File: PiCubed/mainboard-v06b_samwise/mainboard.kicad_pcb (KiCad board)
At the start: 4 copper layers, 90.2 x 95.9 mm, 204 parts, among them J1 503182-1852, J10 35362-0450, J11 MPPT board, J12 35362-0550, J13 USB_C_pycubed, J14 Conn_01x06_Horizontal, J15 35362-0550, J16 1985807, J17 35362-0450, J18 1985807, J19 35362-0650, J2 Conn_ARM_JTAG_SWD_10, J20 35362-0750, J21 35362-0750, J22 QWIIC, J3 35362-0850, J4 35362-0850, J5 35362-1050, J6 35362-0950, J7 Amphenol_901-144, J8 1985807, J9 1985807, Q1 BSS138DWQ-7, Q10 DMP2040USS-13, Q11 MMDT2907, Q15 MBT2222ADW1T1, Q16 MBT2222ADW1T1, Q18 BSS138DWQ-7, Q19 BSS138DWQ-7, Q2 MBT2222ADW1T1, Q21 DMP2040USS-13, Q3 MBT2222ADW1T1, Q4 MBT2222ADW1T1, Q5 IRLML2803, Q6 MMBT2222A-TP, Q7 BSS138DWQ-7, Q8 MBT2222ADW1T1, Q9 IRLML2803, SW1 KMR231NG LFS, U1 MAX706RESA, U16 PE014006, U17 BQ25883RGER, U2 ATSAMD51J20A-AF, U21 TPS7A4501DCQT, U23 RFM98PW, U4 ADM1176-1ARMZ-R7, U5 TPS54226PWPR, U6 LT3652HVIMSE#PBF, U8 MR25H40MDF, Y1 32.768kHz

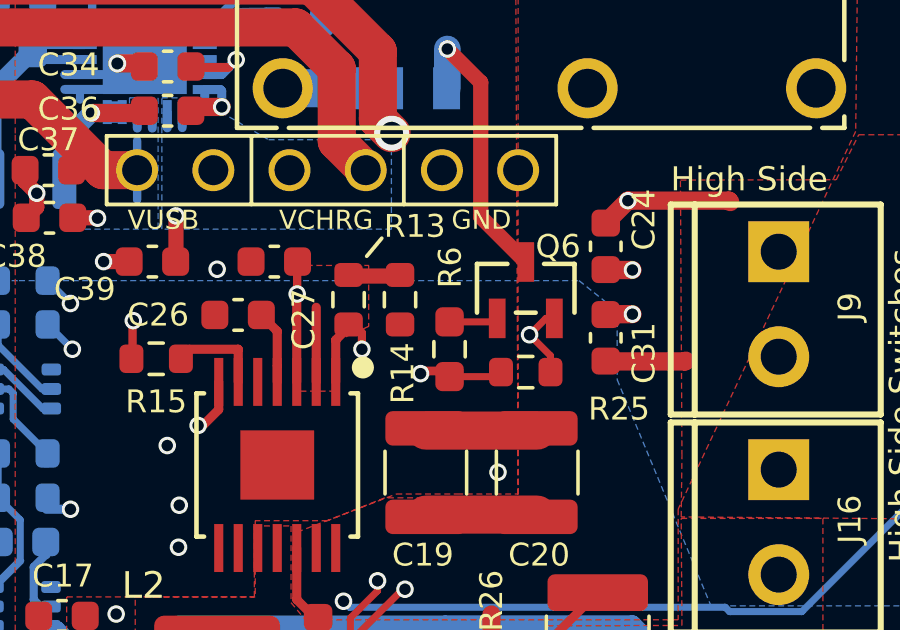
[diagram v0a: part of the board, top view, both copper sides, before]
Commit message: updated interface board, Picubed resistor footprints
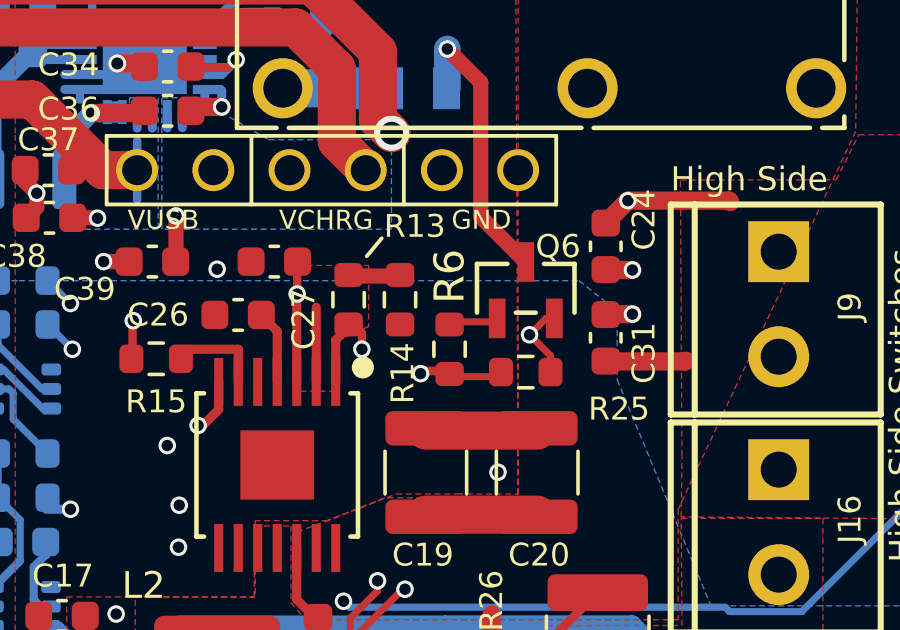
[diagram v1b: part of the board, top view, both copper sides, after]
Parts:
- R6: footprint Resistor_SMD:R_0603_1608Metric_Pad0.98x0.95mm_HandSolder -> Resistor_SMD:R_0603_1608Metric
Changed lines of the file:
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@@
 			)
 		)
-		(property "Description" "22uF +-20% 10V X5R"
+		(property "Description" "Unpolarized capacitor"
 			(at 0 0 0)
 			(layer "F.Fab")
@@
 			)
 		)
+		(property ki_fp_filters "C_*")
 		(sheetname "Power")
 		(sheetfile "Power.kicad_sch")
@@
 			(roundrect_rratio 0.25)
 			(net 1 "GND")
-			(pinfunction "1")
 			(pintype "passive")
 		)
@@
 			(roundrect_rratio 0.25)
 			(net 2 "3.3V")
-			(pinfunction "2")
 			(pintype "passive")
 		)
@@
 			)
 		)
-		(property "Description" "22uF +-20% 10V X5R"
+		(property "Description" "Unpolarized capacitor"
 			(at 0 0 0)
 			(layer "F.Fab")
@@
 			)
 		)
+		(property ki_fp_filters "C_*")
 		(sheetname "Power")
 		(sheetfile "Power.kicad_sch")
@@
 			(roundrect_rratio 0.25)
 			(net 1 "GND")
-			(pinfunction "1")
 			(pintype "passive")
 		)
@@
 			(roundrect_rratio 0.25)
 			(net 2 "3.3V")
-			(pinfunction "2")
 			(pintype "passive")
 		)
@@
 			)
 		)
-		(property "Description" "0.1uF +-10% 50V X7R 0603"
+		(property "Description" "Unpolarized capacitor"
 			(at 244.094 -72.263 0)
 			(layer "F.Fab")
@@
 			)
 		)
+		(property ki_fp_filters "C_*")
 		(sheetname "Power")
 		(sheetfile "Power.kicad_sch")
@@
 			(roundrect_rratio 0.25)
 			(net 17 "Net-(U5-SW1)")
-			(pinfunction "1")
 			(pintype "passive")
 		)
@@
 			(roundrect_rratio 0.25)
 			(net 18 "Net-(U5-VBST)")
-			(pinfunction "2")
 			(pintype "passive")
 		)
@@
 			)
 		)
-		(property "Description" "3.3nF +-10% 100V X7R 0603"
+		(property "Description" "Unpolarized capacitor"
 			(at 311.023 150.114 0)
 			(layer "F.Fab")
@@
 			)
 		)
+		(property ki_fp_filters "C_*")
 		(sheetname "Power")
 		(sheetfile "Power.kicad_sch")
@@
 			(roundrect_rratio 0.25)
 			(net 33 "Net-(U5-SS)")
-			(pinfunction "1")
 			(pintype "passive")
 		)
@@
 			(roundrect_rratio 0.25)
 			(net 1 "GND")
-			(pinfunction "2")
 			(pintype "passive")
 		)
@@
 			(net 1 "GND")
 			(pinfunction "EP")
-			(pintype "bidirectional")
+			(pintype "power_in")
 			(solder_mask_margin 0.0635)
 		)
@@
 			)
 		)
-		(property "Description" "0.1uF +-10% 50V X7R 0603"
+		(property "Description" "Unpolarized capacitor"
 			(at 57.736904 268.653096 0)
 			(layer "F.Fab")
@@
 			)
 		)
+		(property ki_fp_filters "C_*")
 		(sheetname "Connectors")
 		(sheetfile "Connectors.kicad_sch")
@@
 			(roundrect_rratio 0.25)
 			(net 2 "3.3V")
-			(pinfunction "1")
 			(pintype "passive")
 		)
@@
 			(roundrect_rratio 0.25)
 			(net 1 "GND")
-			(pinfunction "2")
 			(pintype "passive")
 		)
@@
 			)
 		)
-		(property "Description" "1uF 0603 X7R"
+		(property "Description" "Unpolarized capacitor"
 			(at 313.436 146.558 0)
 			(layer "F.Fab")
@@
 			)
 		)
+		(property ki_fp_filters "C_*")
 		(sheetname "Power")
 		(sheetfile "Power.kicad_sch")
@@
 			(roundrect_rratio 0.25)
 			(net 34 "Net-(U5-VREG5)")
-			(pinfunction "1")
 			(pintype "passive")
 		)
@@
 			(roundrect_rratio 0.25)
 			(net 1 "GND")
-			(pinfunction "2")
 			(pintype "passive")
 		)
@@
 			)
 		)
-		(property "Description" "10uF +-20% 50V X7R"
+		(property "Description" "Unpolarized capacitor"
 			(at 242.081196 -81.457004 0)
 			(layer "F.Fab")
@@
 			)
 		)
+		(property ki_fp_filters "C_*")
 		(sheetname "Power")
 		(sheetfile "Power.kicad_sch")
@@
 			(roundrect_rratio 0.217391)
 			(net 8 "VBATT")
-			(pinfunction "1")
 			(pintype "passive")
 		)
@@
 			(roundrect_rratio 0.217391)
 			(net 1 "GND")
-			(pinfunction "2")
 			(pintype "passive")
 		)
@@
 			)
 		)
-		(property "Description" "10uF +-20% 50V X7R"
+		(property "Description" "Unpolarized capacitor"
 			(at 245.793096 -85.168904 0)
 			(layer "F.Fab")
@@
 			)
 		)
+		(property ki_fp_filters "C_*")
 		(sheetname "Power")
 		(sheetfile "Power.kicad_sch")
@@
 			(roundrect_rratio 0.217391)
 			(net 8 "VBATT")
-			(pinfunction "1")
 			(pintype "passive")
 		)
@@
 			(roundrect_rratio 0.217391)
 			(net 1 "GND")
-			(pinfunction "2")
 			(pintype "passive")
 		)
@@
 			(net 162 "/Power/V_RF")
 			(pinfunction "OUT")
-			(pintype "output")
+			(pintype "power_out")
 		)
 		(pad "5" smd rect
@@
 		)
 	)
-	(footprint "Resistor_SMD:R_0603_1608Metric_Pad0.98x0.95mm_HandSolder"
+	(footprint "Resistor_SMD:R_0603_1608Metric"
 		(layer "F.Cu")
 		(at 162.56 76.2 90)
-		(descr "Resistor SMD 0603 (1608 Metric), square (rectangular) end terminal, IPC_7351 nominal with elongated pad for handsoldering. (Body size source: IPC-SM-782 page 72, https://www.pcb-3d.com/wordpress/wp-content/uploads/ipc-sm-782a_amendment_1_and_2.pdf), generated with kicad-footprint-generator")
-		(tags "resistor handsolder")
+		(descr "Resistor SMD 0603 (1608 Metric), square (rectangular) end terminal, IPC_7351 nominal, (Body size source: IPC-SM-782 page 72, https://www.pcb-3d.com/wordpress/wp-content/uploads/ipc-sm-782a_amendment_1_and_2.pdf), generated with kicad-footprint-generator")
+		(tags "resistor")
 		(property "Reference" "R6"
-			(at 2.73 0.02 90)
+			(at 2.43 0 90)
 			(layer "F.SilkS")
 			(effects
 				(font
-					(size 0.762 0.762)
-					(thickness 0.127)
+					(size 1 1)
+					(thickness 0.15)
 				)
 			)
@@
 			)
 		)
-		(property "Footprint" "Resistor_SMD:R_0603_1608Metric_Pad0.98x0.95mm_HandSolder"
+		(property "Footprint" "Resistor_SMD:R_0603_1608Metric"
 			(at 0 0 90)
+			(unlocked yes)
 			(layer "F.Fab")
 			(hide yes)
@@
 		(property "Datasheet" ""
 			(at 0 0 90)
+			(unlocked yes)
 			(layer "F.Fab")
 			(hide yes)
@@
 		(property "Description" ""
 			(at 0 0 90)
+			(unlocked yes)
 			(layer "F.Fab")
 			(hide yes)
@@
 		(attr smd)
 		(fp_line
-			(start -0.254724 -0.5225)
-			(end 0.254724 -0.5225)
+			(start -0.237258 -0.5225)
+			(end 0.237258 -0.5225)
 			(stroke
 				(width 0.12)
@@
 		)
 		(fp_line
-			(start -0.254724 0.5225)
-			(end 0.254724 0.5225)
+			(start -0.237258 0.5225)
+			(end 0.237258 0.5225)
 			(stroke
 				(width 0.12)
@@
 		)
 		(fp_line
-			(start 1.65 -0.73)
-			(end 1.65 0.73)
+			(start 1.48 -0.73)
+			(end 1.48 0.73)
 			(stroke
 				(width 0.05)
@@
 		)
 		(fp_line
-			(start -1.65 -0.73)
-			(end 1.65 -0.73)
+			(start -1.48 -0.73)
+			(end 1.48 -0.73)
 			(stroke
 				(width 0.05)
@@
 		)
 		(fp_line
-			(start 1.65 0.73)
-			(end -1.65 0.73)
+			(start 1.48 0.73)
+			(end -1.48 0.73)
 			(stroke
 				(width 0.05)
@@
 		)
 		(fp_line
-			(start -1.65 0.73)
-			(end -1.65 -0.73)
+			(start -1.48 0.73)
+			(end -1.48 -0.73)
 			(stroke
 				(width 0.05)
@@
 		)
 		(pad "1" smd roundrect
-			(at -0.9125 0 90)
-			(size 0.975 0.95)
+			(at -0.825 0 90)
+			(size 0.8 0.95)
 			(layers "F.Cu" "F.Paste" "F.Mask")
 			(roundrect_rratio 0.25)
@@
 		)
 		(pad "2" smd roundrect
-			(at 0.9125 0 90)
-			(size 0.975 0.95)
+			(at 0.825 0 90)
+			(size 0.8 0.95)
 			(layers "F.Cu" "F.Paste" "F.Mask")
 			(roundrect_rratio 0.25)
@@
 		(at 147.55 142.92 180)
 		(property "Reference" "J10"
-			(at 4 -2.43 360)
+			(at 4 -2.43 0)
 			(layer "F.SilkS")
 			(effects
@@
 		)
 		(property "Value" "35362-0450"
-			(at -7.01 -4.815 360)
+			(at -7.01 -4.815 0)
 			(layer "F.Fab")
 			(effects
@@
 		)
 		(property "Footprint" "ssi_connector:Molex_35362-0450"
-			(at -3 0 360)
+			(at -3 0 0)
 			(layer "F.Fab")
 			(hide yes)
@@
 		)
 		(property "Datasheet" ""
-			(at -3 0 360)
+			(at -3 0 0)
 			(layer "F.Fab")
 			(hide yes)
@@
 		)
 		(property "Description" ""
-			(at -3 0 360)
+			(at -3 0 0)
 			(layer "F.Fab")
 			(hide yes)
@@
 		(at 171.55 142.92 180)
 		(property "Reference" "J17"
-			(at -8.9 -3.98 360)
+			(at -8.9 -3.98 0)
 			(layer "F.SilkS")
 			(effects
@@
 		)
 		(property "Value" "35362-0450"
-			(at -7.01 -4.815 360)
+			(at -7.01 -4.815 0)
 			(layer "F.Fab")
 			(effects
@@
 		)
 		(property "Footprint" "ssi_connector:Molex_35362-0450"
-			(at -3 0 360)
+			(at -3 0 0)
 			(layer "F.Fab")
 			(hide yes)
@@
 		)
 		(property "Datasheet" ""
-			(at -3 0 360)
+			(at -3 0 0)
 			(layer "F.Fab")
 			(hide yes)
@@
 		)
 		(property "Description" ""
-			(at -3 0 360)
+			(at -3 0 0)
 			(layer "F.Fab")
 			(hide yes)

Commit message: updated XY coils to kicad v8
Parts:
- G*** (x3): value SSI_logo_medium -> logo_SSI_medium; footprint ssi_drawings:SSI_logo_medium -> ssi_drawings:logo_SSI_medium
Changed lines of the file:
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@@
 		)
 	)
-	(footprint "ssi_drawings:SSI_logo_medium"
+	(footprint "ssi_drawings:logo_SSI_medium"
 		(layer "F.Cu")
 		(at 152.24 123.79)
@@
 			)
 		)
-		(property "Value" "SSI_logo_medium"
+		(property "Value" "logo_SSI_medium"
 			(at 0.75 0 0)
 			(layer "F.SilkS")
@@
 			)
 		)
-		(property "Footprint" "ssi_drawings:SSI_logo_medium"
+		(property "Footprint" "ssi_drawings:logo_SSI_medium"
 			(at 0 0 0)
 			(layer "F.Fab")
@@
 		)
 	)
-	(footprint "ssi_drawings:SSI_logo_medium"
+	(footprint "ssi_drawings:logo_SSI_medium"
 		(layer "B.Cu")
 		(at 160.84294 125.054203 180)
@@
 			)
 		)
-		(property "Value" "SSI_logo_medium"
+		(property "Value" "logo_SSI_medium"
 			(at 0.75 0 0)
 			(layer "B.SilkS")
@@
 			)
 		)
-		(property "Footprint" "ssi_drawings:SSI_logo_medium"
+		(property "Footprint" "ssi_drawings:logo_SSI_medium"
 			(at 0 0 0)
 			(layer "B.Fab")
@@
 		)
 	)
-	(footprint "ssi_drawings:SSI_logo_medium"
+	(footprint "ssi_drawings:logo_SSI_medium"
 		(layer "B.Cu")
 		(at 106.925528 108.794051 180)
@@
 			)
 		)
-		(property "Value" "SSI_logo_medium"
+		(property "Value" "logo_SSI_medium"
 			(at 0.75 0 0)
 			(layer "B.SilkS")
@@
 			)
 		)
-		(property "Footprint" "ssi_drawings:SSI_logo_medium"
+		(property "Footprint" "ssi_drawings:logo_SSI_medium"
 			(at 0 0 0)
 			(layer "B.Fab")

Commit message: updated with durand-groundstation components, cleaned up libraries
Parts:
- G***: value logo_SSI_medium -> stanford_seal; footprint ssi_drawings:logo_SSI_medium -> ssi_drawings:stanford_seal
- G***: value logo_SSI_medium -> redwood; footprint ssi_drawings:logo_SSI_medium -> ssi_drawings:redwood
- Q1, Q18, Q19, Q7: value BSS138DWQ-7 -> SOT65P210X110-6N
- U4: value ADM1176-1ARMZ-R7 -> RM_10
- moved G*** 1.56 mm to (105.4, 108.8)

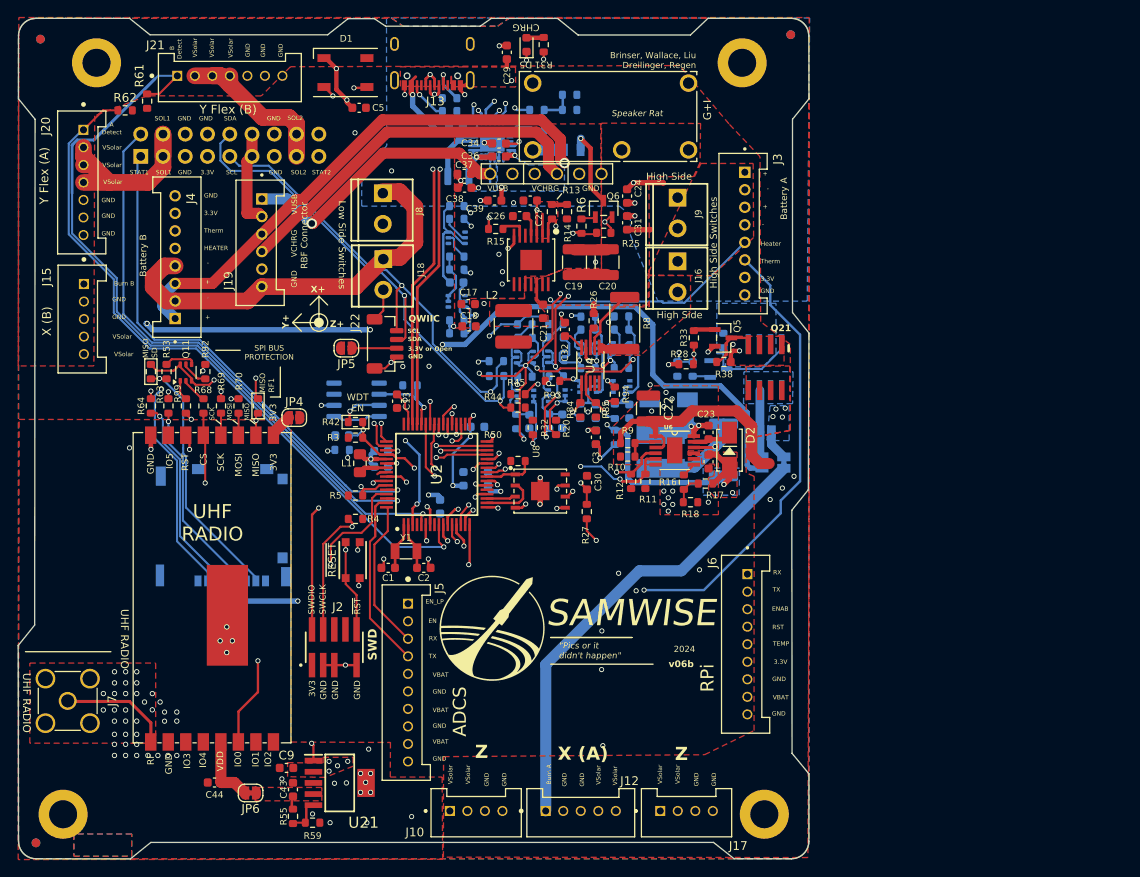
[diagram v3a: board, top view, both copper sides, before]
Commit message: Change: SAMD replacement part 4
Started layout of new components
Swapped some pins around on the RP2350B for simpler layout
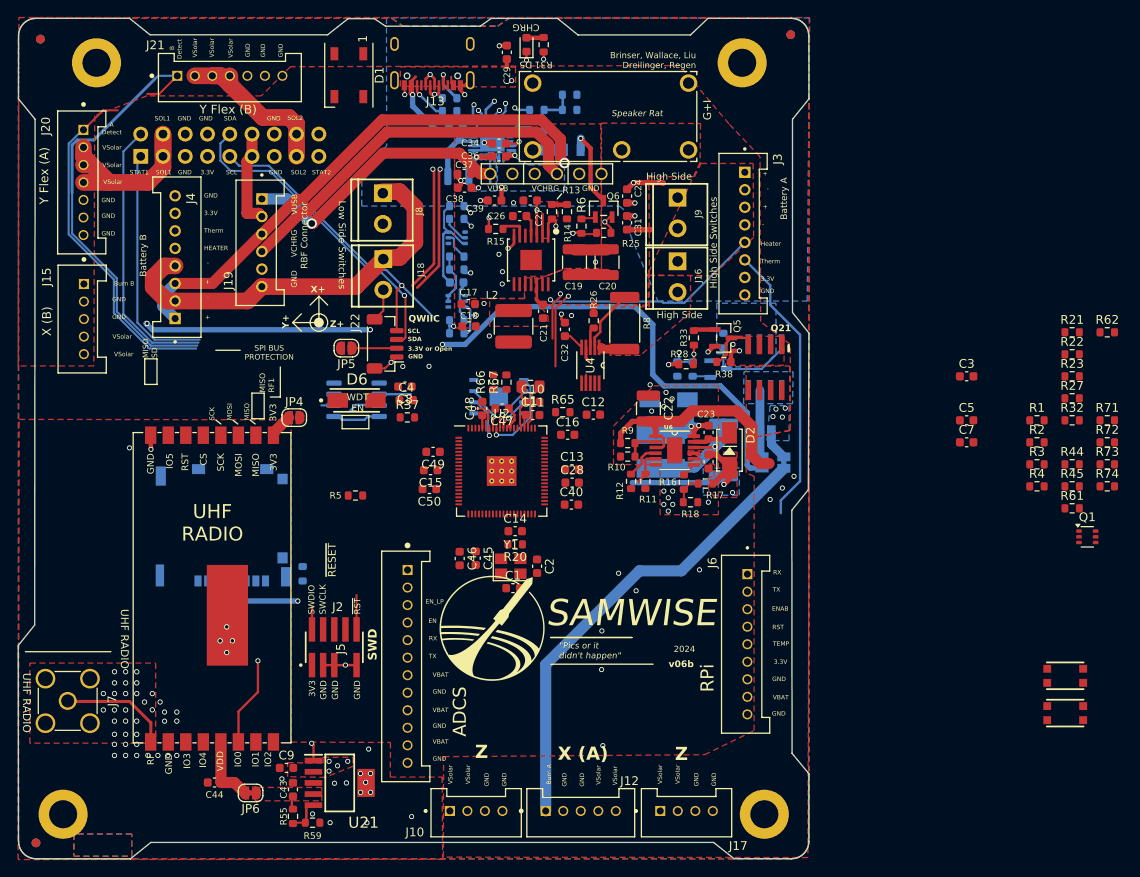
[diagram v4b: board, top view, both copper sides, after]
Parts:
- removed C30: 0.1uF, Capacitor_SMD:C_0603_1608Metric
- removed C41, C42: 10nF, Capacitor_SMD:C_0603_1608Metric
- removed the G*** at (160.8, 125.1)
- removed Q11: MMDT2907, Package_TO_SOT_SMD:SOT-363_SC-70-6
- removed Q15, Q16, Q4, Q8: MBT2222ADW1T1, Package_TO_SOT_SMD:SOT-363_SC-70-6
- removed Q18, Q19, Q7: SOT65P210X110-6N, ssi_transistor:BSS138DWQ-7
- removed R101, R104, R108, R109, R53, R54, R56, R99: 0, Resistor_SMD:R_0603_1608Metric
- removed R24, R48, R95, R96: 200k, Resistor_SMD:R_0603_1608Metric
- removed R41, R43, R50, R7, R82, R83, R84, R85: 10k, Resistor_SMD:R_0603_1608Metric
- removed R42: 100, Resistor_SMD:R_0603_1608Metric
- removed R63, R64, R69, R70: 1k, Resistor_SMD:R_0603_1608Metric
- removed R68, R92: 4.7k, Resistor_SMD:R_0603_1608Metric
- removed R86, R87: 680, Resistor_SMD:R_0603_1608Metric
- removed R93, R94: 100k, Resistor_SMD:R_0603_1608Metric
- removed U8: MR25H40MDF, ssi_IC:SON127P600X500X90-9N
- added C28: 0.1uF, Capacitor_SMD:C_0603_1608Metric, F.Cu at (161.5, 105.5)
- added C40: 0.1uF, Capacitor_SMD:C_0603_1608Metric, F.Cu at (161.4, 108.0)
- added C45: 0.1uF, Capacitor_SMD:C_0603_1608Metric, F.Cu at (150.5, 114.1)
- added C46: 0.1uF, Capacitor_SMD:C_0603_1608Metric, F.Cu at (148.7, 114.1)
- added C47: 0.1uF, Capacitor_SMD:C_0603_1608Metric, F.Cu at (153.5, 97.0)
- added C48: 0.1uF, Capacitor_SMD:C_0603_1608Metric, F.Cu at (151.2, 97.0)
- added C49: 0.1uF, Capacitor_SMD:C_0603_1608Metric, F.Cu at (145.6, 102.0)
- added C50: 0.1uF, Capacitor_SMD:C_0603_1608Metric, F.Cu at (145.2, 106.2)
- added D6: CMSH1-40M, ssi_diode:DIOM5226X262N, F.Cu at (136.9, 96.1)
- added R65: 33, Resistor_SMD:R_0603_1608Metric, F.Cu at (160.4, 97.4)
- added R66: 27, Resistor_SMD:R_0603_1608Metric, F.Cu at (152.5, 94.0)
- added R67: 27, Resistor_SMD:R_0603_1608Metric, F.Cu at (154.0, 94.0)
- added R71: 10k, Resistor_SMD:R_0603_1608Metric, F.Cu at (222.6, 98.3)
- added R72: 10k, Resistor_SMD:R_0603_1608Metric, F.Cu at (222.6, 100.9)
- added R73: 10k, Resistor_SMD:R_0603_1608Metric, F.Cu at (222.6, 103.4)
- added R74: 10k, Resistor_SMD:R_0603_1608Metric, F.Cu at (222.6, 105.9)
- added SW2: KMR231NG LFS, ssi_switch:BTN_KMR2_4.6X2.8, F.Cu at (217.8, 131.8)
- added U3: MR25H40MDF, ssi_IC:SON127P600X500X90-9N, B.Cu at (153.1, 95.7)
- C1, C2: value 8pF -> 15p
- C10, C11: value 0.1uF -> 4.7uF; moved to F.Cu
- C12, C15: value 1uF -> 4.7uF; moved to F.Cu
- C13: value 1uF -> 0.1uF
- C14, C16: value 10uF -> 0.1uF; moved to F.Cu
- C4: value 1uF -> 10uF; moved to F.Cu
- C7, C8: value 10nF -> 0.1uF; moved to F.Cu
- J5: value 35362-1050 -> 35362-1250; footprint ssi_connector:Molex_35362-1050 -> ssi_connector:Molex_35362-1250
- Q1: value SOT65P210X110-6N -> MBT2222ADW1T1; footprint ssi_transistor:BSS138DWQ-7 -> Package_TO_SOT_SMD:SOT-363_SC-70-6; moved to F.Cu
- R1, R2, R22: moved to F.Cu
- R20: value 100k -> 1k
- R21: value 680 -> 10k; moved to F.Cu
- R23: value 10k -> 1k; moved to F.Cu
- R3, R4: value 10k -> 1k
- R32: value 100k -> 10k
- R37: value 680 -> 100k; moved to F.Cu
- R52: value 10k -> 0
- U2: value ATSAMD51J20A-AF -> RP2350_80QFN; footprint ssi_IC:QFP50P1200X1200X120-64N -> ssi_IC:RP2350-QFN-80-1EP_10x10_P0.4mm_EP3.4x3.4mm_ThermalVias
- U4: value RM_10 -> ADM1176-1ARMZ-R7
- Y1: value 32.768kHz -> ABM8-272-T3; footprint Crystal:Crystal_SMD_3215-2Pin_3.2x1.5mm -> Crystal:Crystal_SMD_3225-4Pin_3.2x2.5mm
- moved R61 115.3 mm to (218.5, 108.4), turned to 0 degrees
- moved R62 114.9 mm to (222.6, 88.3), turned to 0 degrees
- moved SW1 82.4 mm to (217.8, 127.5), turned to 0 degrees
- moved C5 77.9 mm to (206.5, 98.3), turned to 0 degrees
- moved R4 77.8 mm to (214.5, 105.9), turned to 0 degrees
- moved R3 77.8 mm to (214.5, 103.4)
- moved R45 64.1 mm to (218.5, 105.9)
- moved R44 63.5 mm to (218.5, 103.4), turned to 0 degrees
- moved Q1 62.6 mm to (220.3, 111.6), turned to 0 degrees
- moved R32 61.5 mm to (218.5, 98.3), turned to 0 degrees
- moved R22 59.0 mm to (218.5, 90.8)
- moved R21 58.9 mm to (218.5, 88.3), turned to 0 degrees
- moved R23 58.8 mm to (218.5, 93.3)
- moved R27 56.9 mm to (218.5, 95.8), turned to 0 degrees
- moved R2 50.3 mm to (214.5, 100.9), turned to 0 degrees
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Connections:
- net VCC_RF1 renamed RF_VCC
- C10 pad 1: 3.3V -> +1V1
- C11 pad 1: 3.3V -> +3.3V
- C12 pad 1: GND -> Net-(U2-VREG_AVDD)
- C12 pad 2: Net-(U2-VDDCORE) -> GND
- C13 pad 1: 3.3V -> +1V1
- C14 pad 1: Net-(U2-VDDCORE) -> +1V1
- C15 pad 1: 3.3V -> +1V1
- C16 pad 1: 3.3V -> +3.3V
- C2 pad 1: /Avionics/XTAL2 -> Net-(C2-Pad1)
- C37 pad 2: Net-(J14-Pin_1) -> Net-(J14-Pin_3)
- C38 pad 2: Net-(J14-Pin_1) -> Net-(J14-Pin_3)
- C39 pad 2: Net-(J14-Pin_4) -> Net-(J14-Pin_6)
- C4 pad 2: ~{RESET} -> /Avionics/WDT_VCC
- C7 pad 1: Net-(Q1B-G1) -> 3.3V
- C8 pad 1: Net-(Q7B-G1) -> /Avionics/WDT_VCC
- D1 pad 4: Net-(D1-DIN) -> /Avionics/NEOPIXEL
- J1 pad 3: MOSI_SD -> SD_MOSI
- J1 pad 5: SCK_SD -> SD_SCK
- J1 pad 7: MISO_SD -> SD_MISO
- J19 pad 1: Net-(J14-Pin_1) -> RBF_DETECT
- J19 pad 4: Net-(J14-Pin_4) -> Net-(J14-Pin_6)
- J5 pad 1: ADCS_EN_LP -> ADCS_POR
- J5 pad 2: ADCS_EN -> ADCS_EN_LP
- J5 pad 3: ADCS_Rx -> ADCS_EN
- J5 pad 4: ADCS_Tx -> ADCS_PGOOD
- J5 pad 5: VBATT -> ADCS_Tx
- J5 pad 6: GND -> ADCS_Rx
- L1 pad 1: Net-(U2-VDDCORE) -> Net-(U2-VREG_LX)
- L1 pad 2: Net-(U2-VSW) -> +1V1
- Q1 pad 2: Net-(Q1A-G2) -> GND
- Q1 pad 3: Net-(Q1A-G2) -> VBUS_RESET
- Q1 pad 5: Net-(Q1B-G1) -> Net-(Q1B-B2)
- Q1 pad 6: Net-(Q1A-D1) -> GND
- R20 pad 1: 3.3V -> Net-(C2-Pad1)
- R20 pad 2: Net-(Q1A-G2) -> /Avionics/XTAL2
- R21 pad 1: Net-(Q4A-B1) -> /Avionics/FLASH_CS
- R21 pad 2: Net-(Q1A-D1) -> 3.3V
- R22 pad 2: Net-(Q1A-D1) -> RBF_DETECT
- R23 pad 1: 3.3V -> ~{RESET}
- R23 pad 2: SCL_PWR2 -> /Avionics/RUN
- R27 pad 1: GND -> 3.3V
- R27 pad 2: RPI_RST -> SideDeplyDetectB
- R3 pad 1: 3.3V -> Net-(SW1-P)
- R3 pad 2: ~{RESET} -> /Avionics/RUN
- R32 pad 1: 3.3V -> Net-(Q1B-B2)
- R32 pad 2: Net-(Q7A-G2) -> Net-(U1-~{WDO})
- R37 pad 1: Net-(Q8A-B1) -> VBUS_RESET
- R37 pad 2: Net-(Q7A-D1) -> /Avionics/WDT_VCC
- R4 pad 1: 3.3V -> Net-(SW2-P)
- R4 pad 2: SWCLK -> /Avionics/FLASH_CS
- R5 pad 2: RF1_CS -> RF_CS
- R61 pad 1: 3.3V -> GND
- R61 pad 2: SideDeplyDetectB -> RPI_RST
- SW1 pad A: ~{RESET} -> Net-(SW1-P)
- SW1 pad A': ~{RESET} -> Net-(SW1-P)
- U1 pad 1: Net-(U1-~{MR}) -> unconnected-(U1-~{MR}-Pad1)
- U1 pad 2: 3.3V -> /Avionics/WDT_VCC
- U1 pad 6: WDT_WDI -> /Avionics/WDI
- U1 pad 7: Net-(U1-~{RESET}) -> unconnected-(U1-~{RESET}-Pad7)
- U1 pad 8: Net-(U1-~{MR}) -> Net-(U1-~{WDO})
- U17 pad 13: Net-(J14-Pin_4) -> Net-(J14-Pin_6)
- U17 pad 14: Net-(J14-Pin_4) -> Net-(J14-Pin_6)
- U17 pad 15: Net-(J14-Pin_1) -> Net-(J14-Pin_3)
- U17 pad 16: Net-(J14-Pin_1) -> Net-(J14-Pin_3)
- U2 pad 1: /Avionics/XTAL1 -> SDA
- U2 pad 10: RPI_ENAB -> +1V1
- U2 pad 11: ~{FIXED_SOLAR_CHRG} -> RF_MISO
- U2 pad 12: RPI_RST -> RF_CS
- U2 pad 13: RPI_TEMP -> RF_SCK
- U2 pad 14: ENAB_BURN_B -> RF_MOSI
- U2 pad 15: /Avionics/BATTERY -> +3.3V
- U2 pad 16: SENSE_THERM_A -> SD_MISO
- U2 pad 17: FLASH_MOSI -> SD_CS
- U2 pad 18: FLASH_MISO -> SD_SCK
- U2 pad 19: FLASH_IO2 -> SD_MOSI
- U2 pad 2: /Avionics/XTAL2 -> SCL
- U2 pad 20: FLASH_IO3 -> RF_IO0
- U2 pad 21: 3.3V -> ENAB_RF
- U2 pad 22: GND -> ADCS_EN
- U2 pad 23: FLASH_SCK -> ADCS_EN_LP
- U2 pad 24: FLASH_CS -> +3.3V
- U2 pad 25: SDA -> ADCS_Tx
- U2 pad 26: SCL -> ADCS_Rx
- U2 pad 27: ~{FIXED_SOLAR_FAULT} -> ADCS_PGOOD
- U2 pad 28: BURN_RELAY_A -> ADCS_POR
- U2 pad 29: MOSI -> +3.3V
- U2 pad 3: SENSE_THERM_B -> /Avionics/WDI
- U2 pad 30: SCK -> /Avionics/XTAL1
- U2 pad 31: MISO -> /Avionics/XTAL2
- U2 pad 32: ENAB_BURN_A -> +1V1
- U2 pad 33: GND -> SWCLK
- U2 pad 34: 3.3V -> SWDIO
- U2 pad 35: RPI_UART_TO_PI -> /Avionics/RUN
- U2 pad 36: RPI_UART_FROM_PI -> unconnected-(U2-GPIO28-Pad36)
- U2 pad 37: VBUS_RESET -> RPI_ENAB
- U2 pad 38: RF1_RST -> RPI_UART_TO_PI
- U2 pad 39: BAT_HEATER_A -> RPI_UART_FROM_PI
- U2 pad 4: 3.3V -> ~{MPPT_SHDN_1}
- U2 pad 40: BAT_HEATER_B -> RPI_RST
- U2 pad 41: ADCS_EN_LP -> +3.3V
- U2 pad 42: Net-(D1-DIN) -> ~{FIXED_SOLAR_CHRG}
- U2 pad 43: ADCS_EN -> ~{FIXED_SOLAR_FAULT}
- U2 pad 44: WDT_WDI -> ENAB_BURN_B
- U2 pad 45: USB_D- -> ENAB_BURN_A
- U2 pad 46: USB_D+ -> BAT_HEATER_A
- U2 pad 47: GND -> SDA_PWR
- U2 pad 48: 3.3V -> SCL_PWR
- U2 pad 49: MPPT_STAT_2 -> RPI_TEMP
- U2 pad 5: SideDeplyDetectB -> +3.3V
- U2 pad 50: ~{MPPT_SHDN_2} -> +3.3V
- U2 pad 51: SD_CS -> +1V1
- U2 pad 52: ~{RESET} -> SENSE_THERM_A
- U2 pad 53: Net-(U2-VDDCORE) -> BURN_RELAY_A
- U2 pad 54: GND -> RBF_DETECT
- U2 pad 55: Net-(U2-VSW) -> /Avionics/BATTERY
- U2 pad 56: 3.3V -> SDA_PWR2
- U2 pad 57: SWCLK -> SCL_PWR2
- U2 pad 58: SWDIO -> SENSE_THERM_B
- U2 pad 59: RF1_CS -> +3.3V
- U2 pad 6: ENAB_RF -> MPPT_STAT_1
- U2 pad 60: MPPT_STAT_1 -> +3.3V
- U2 pad 61: RF1_IO0 -> Net-(U2-VREG_AVDD)
- U2 pad 62: ~{MPPT_SHDN_1} -> GND
- U2 pad 63: ADCS_Tx -> Net-(U2-VREG_LX)
- U2 pad 64: ADCS_Rx -> +3.3V
- U2 pad 7: GND -> RF_RST
- U2 pad 8: 3.3V -> SideDeplyDetectA
- U2 pad 9: SideDeplyDetectA -> SideDeplyDetectB
- U23 pad 10: MISO_RF1 -> RF_MISO
- U23 pad 11: MOSI_RF1 -> RF_MOSI
- U23 pad 12: SCK_RF1 -> RF_SCK
- U23 pad 13: RF1_CS -> RF_CS
- U23 pad 14: RF1_RST -> RF_RST
- U23 pad 6: RF1_IO0 -> RF_IO0
- Y1 pad 2: /Avionics/XTAL2 -> GND
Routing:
- net SDA: track 103.8 -> 36.8 mm, vias 5 -> 1
- net SD_CS: track 60.0 -> 0.00 mm, vias 4 -> 0
- net 3.3V: track 112.2 -> 53.8 mm, vias 21 -> 7
- net SCL: track 90.6 -> 36.1 mm, vias 5 -> 1
- net RPI_UART_TO_PI: track 50.3 -> 0.00 mm, vias 1 -> 0
- net RPI_UART_FROM_PI: track 47.6 -> 0.00 mm, vias 1 -> 0
- net MISO: track 45.9 -> 0.00 mm, vias 3 -> 0
- net SENSE_THERM_A: track 77.5 -> 32.4 mm, vias 2 -> 0
- net MOSI: track 44.5 -> 0.00 mm, vias 3 -> 0
- net Net-(D1-DIN): track 44.2 -> 0.00 mm, vias 2 -> 0
- net SENSE_THERM_B: track 51.8 -> 9.35 mm, vias 2 -> 0
- net SCK: track 42.5 -> 0.00 mm, vias 3 -> 0
- net RPI_RST: track 42.4 -> 0.00 mm, vias 2 -> 0
- net SideDeplyDetectA: track 80.1 -> 39.7 mm, vias 1 -> 0
- net RPI_ENAB: track 40.1 -> 0.00 mm, vias 1 -> 0
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- added copper zone on B.Cu, net Net-(J14-Pin_3)
- added copper zone on B.Cu, net Net-(J14-Pin_6)
- removed copper zone on B.Cu, net Net-(J14-Pin_1)
- removed copper zone on B.Cu, net Net-(J14-Pin_4)
